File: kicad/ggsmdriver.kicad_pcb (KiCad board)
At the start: 4 copper layers, 55 x 45 mm, 65 parts, among them J3 VIN GND A2 A1 B1 B2, J4 EXP, J5 USB-C, SW1 BOOT, SW2 RESET, U1 STM32G0B1CBT6, U2 TMC2209-LA-T, U3 TPS54202DDCR, U4 XC6206P332MR, U5 USBLC6-2SC6

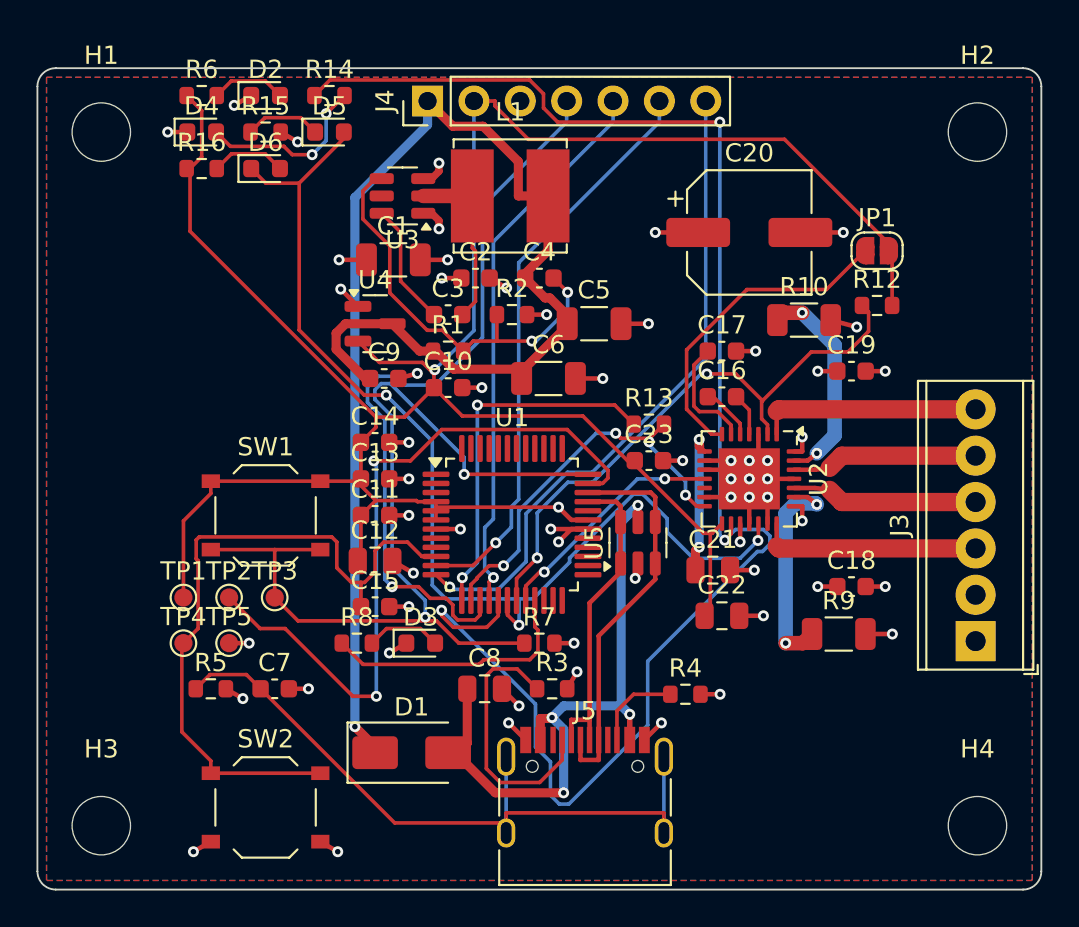
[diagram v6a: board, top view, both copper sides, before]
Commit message: LEDs in a labelled column at the top-right, re-routed
D2-D6 stacked at x 49.9 with PWR/STAT/STEP/DIR+/DIR- silk labels; their
resistors moved below J3. 0 unrouted, no DRC errors; fab regenerated.
Docs record where the 75 pF and 220 nF values came from.

Co-Authored-By: Claude Opus 5.5 (1M context) <noreply@anthropic.com>
Claude-Session: https://claude.ai/code/session_01VFhb1Qv7mkaGrgvtw2CS4q
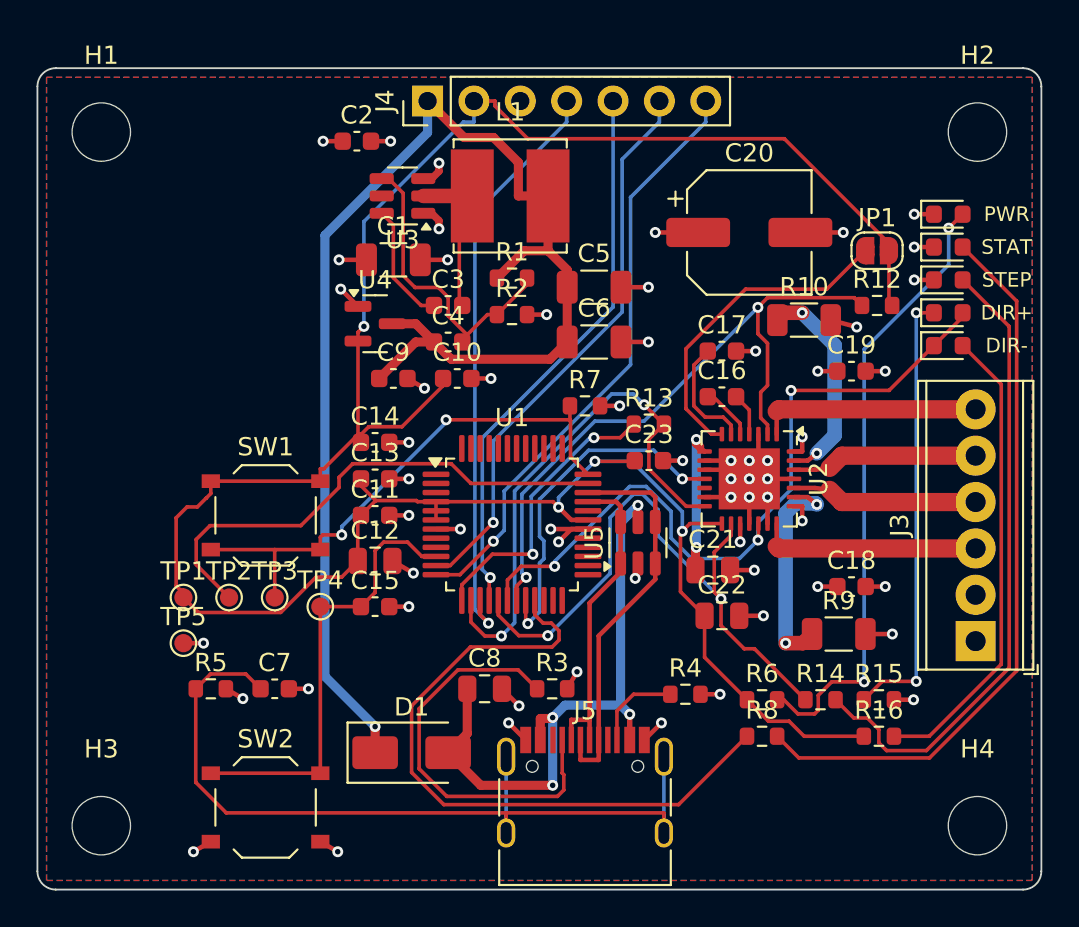
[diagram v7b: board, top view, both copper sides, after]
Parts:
- moved R16 48.4 mm to (146.1, 136.6)
- moved R15 45.8 mm to (146.1, 134.6)
- moved R6 45.1 mm to (139.7, 134.6)
- moved R14 42.7 mm to (142.9, 134.6)
- moved D4 41.7 mm to (149.9, 111.6)
- moved D6 38.6 mm to (149.9, 115.2)
- moved D2 38.0 mm to (149.9, 108.0)
- moved D3 36.1 mm to (149.9, 109.8)
- moved D5 35.3 mm to (149.9, 113.4)
- moved R8 22.8 mm to (139.7, 136.6)
- moved R7 13.2 mm to (130.0, 118.5)
- moved C2 9.92 mm to (117.5, 104.0)
- moved TP4 7.76 mm to (115.5, 129.5)
- moved C4 6.10 mm to (122.5, 115.0)
- moved R1 5.32 mm to (126.0, 111.5)
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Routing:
- net TMC_STEP: track 88.9 -> 34.1 mm, vias 3 -> 2
- net LED_STAT: track 4.12 -> 40.0 mm
- net LED_PWR: track 4.12 -> 34.2 mm, vias 0 -> 2
- net LED_STEP: track 9.76 -> 35.3 mm, vias 2 -> 0
- net LED_STAT_R: track 14.4 -> 36.9 mm
- net LED_DIRL: track 4.13 -> 25.8 mm
- net BOOT0_SWCLK: track 51.6 -> 30.1 mm
- net LED_DIRH: track 4.19 -> 24.4 mm, vias 0 -> 2
- net TMC_DIR: track 59.5 -> 41.2 mm
- net NRST: track 38.2 -> 24.6 mm
- net SWDIO: track 39.4 -> 27.9 mm, vias 2 -> 0
- net IO1: track 41.0 -> 32.4 mm
- net USB_CC1: track 14.6 -> 22.5 mm
- net TMC_UART: track 21.9 -> 29.2 mm, vias 4 -> 2
- net TMC_DIAG: track 13.0 -> 19.4 mm
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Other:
- board text added: "DIR+"
- board text added: "DIR-"
- board text added: "PWR"
- board text added: "STAT"
- board text added: "STEP"

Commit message: LEDs to the left side, C4 back to 75 pF, tidy silkscreen designators
LED column now on the left with facing pads and hand tracks; designators
placed by autopcb tidy_silk(). 0 unrouted, DRC clean; fab regenerated.

Co-Authored-By: Claude Opus 5.5 (1M context) <noreply@anthropic.com>
Claude-Session: https://claude.ai/code/session_01VFhb1Qv7mkaGrgvtw2CS4q
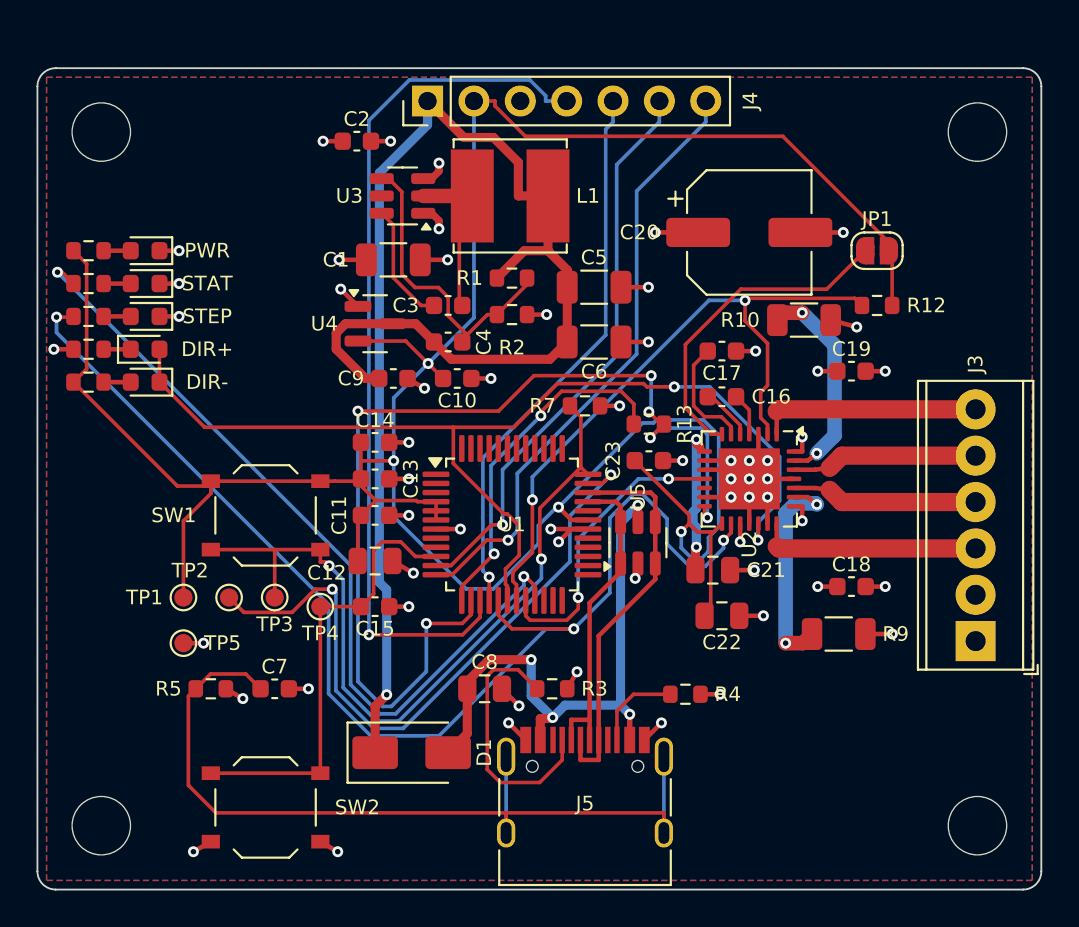
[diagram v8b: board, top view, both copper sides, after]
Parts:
- C4: value 100pF -> 75pF
- moved R16 47.4 mm to (102.8, 117.2)
- moved R15 47.4 mm to (102.8, 115.4), turned to 180 degrees
- moved R14 45.3 mm to (102.8, 113.6)
- moved R8 44.5 mm to (102.8, 111.8)
- moved R6 44.3 mm to (102.8, 110.0)
- moved D2 44.0 mm to (105.9, 110.0), turned to 180 degrees
- moved D3 44.0 mm to (105.9, 111.8), turned to 180 degrees
- moved D4 44.0 mm to (105.9, 113.6), turned to 180 degrees
- moved D5 44.0 mm to (105.9, 115.4)
- moved D6 44.0 mm to (105.9, 117.2), turned to 180 degrees
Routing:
- net LED_STAT: track 40.0 -> 1.49 mm
- net LED_STEP: track 35.3 -> 1.49 mm
- net TMC_STEP: track 34.1 -> 67.9 mm, vias 2 -> 3
- net LED_PWR: track 34.2 -> 1.49 mm, vias 2 -> 0
- net TMC_UART: track 29.2 -> 55.7 mm, vias 2 -> 6
- net LED_DIRL: track 25.8 -> 1.49 mm
- net LED_DIRH: track 24.4 -> 1.49 mm, vias 2 -> 0
- net +3V3: track 137.0 -> 153.7 mm
- net TMC_DIR: track 41.2 -> 56.9 mm, vias 3 -> 2
- net IO1: track 32.4 -> 48.0 mm
- net BOOT0_SWCLK: track 30.1 -> 42.9 mm
- net SWDIO: track 27.9 -> 36.7 mm, vias 0 -> 2
- net LED_STAT_R: track 36.9 -> 45.5 mm, vias 0 -> 2
- net USB_CC1: track 22.5 -> 14.4 mm
- net TMC_TX: track 15.9 -> 19.2 mm
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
